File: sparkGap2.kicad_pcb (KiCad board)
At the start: 4 copper layers, 53.1 x 54.1 mm, 47 parts, among them J1 9V, J2 IN, J3 OUT, Q1 BS170, SW1 SPST, SW2 6-pin Footswitch, U1 TL072

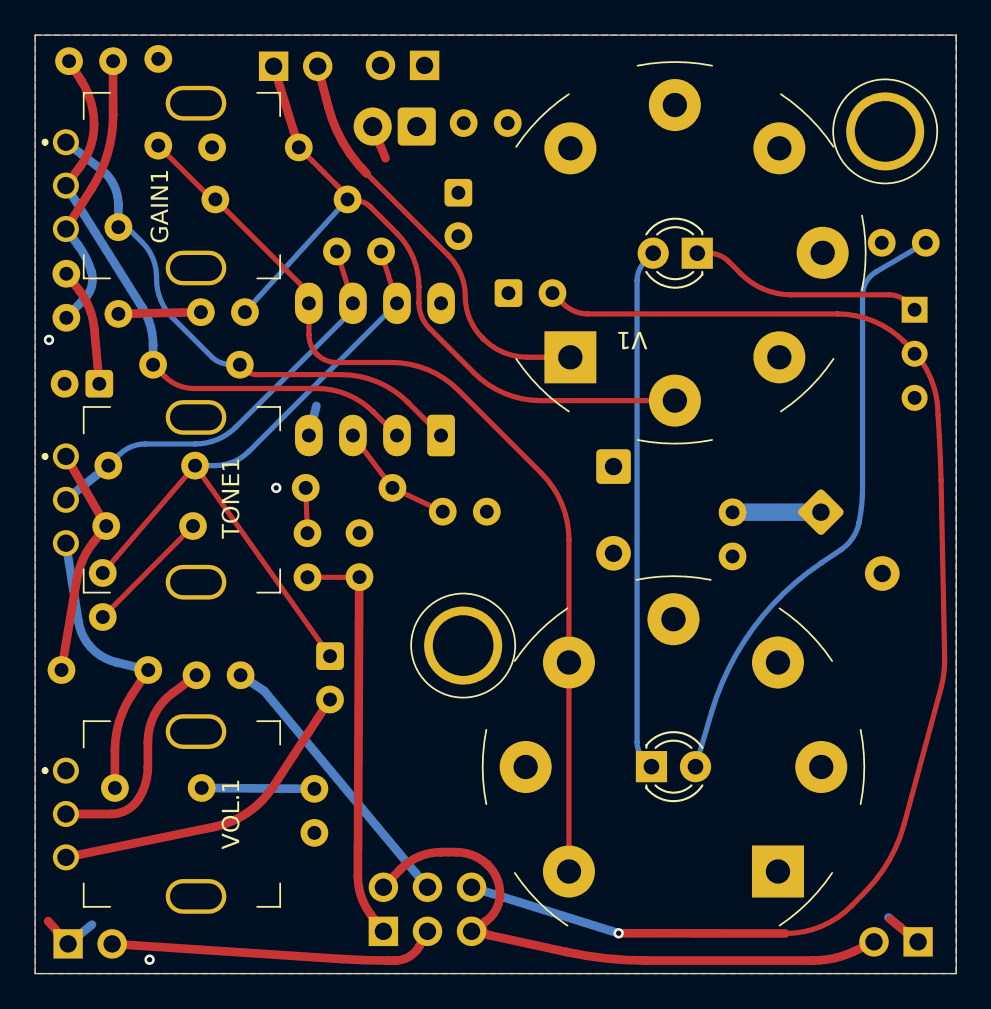
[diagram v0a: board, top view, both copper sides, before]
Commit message: Clean up footprints and schematic to get rid of warnings
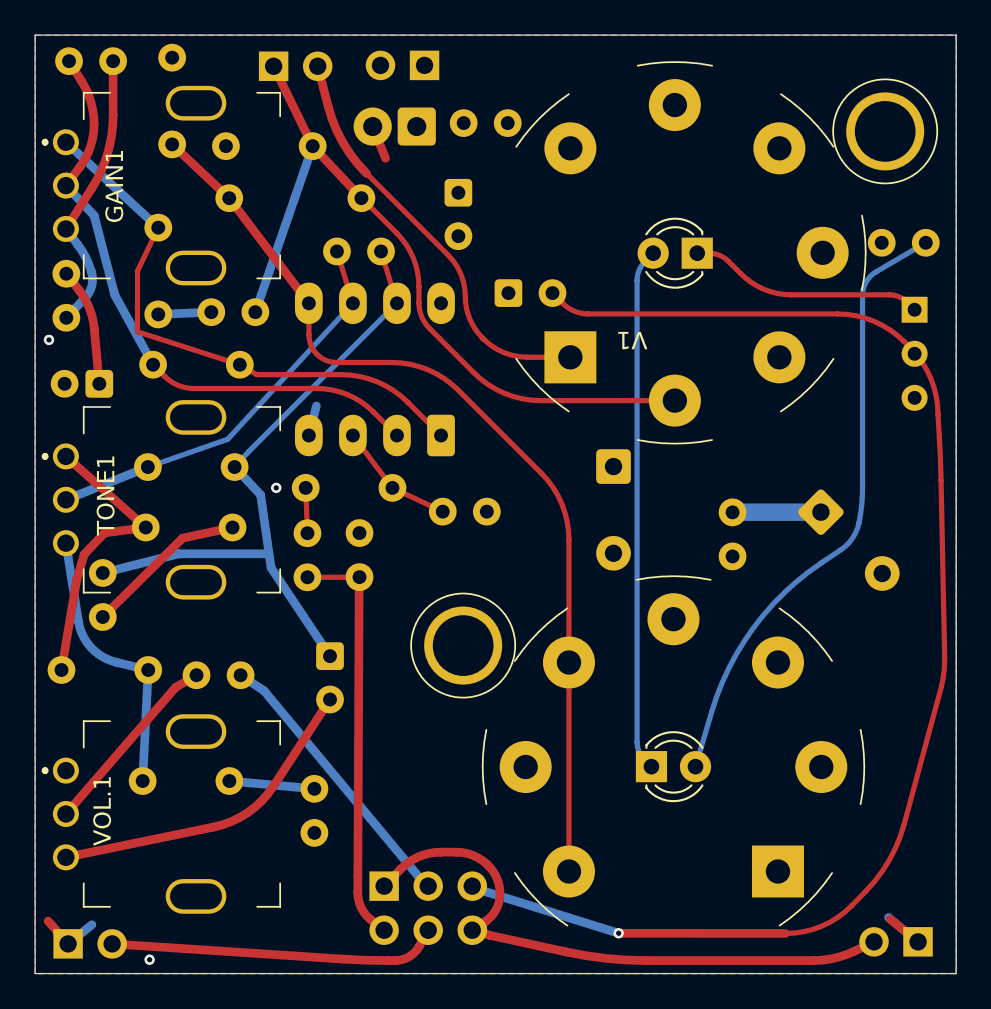
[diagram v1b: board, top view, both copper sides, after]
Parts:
- Mount1, Mount2: renamed from REF**; value B9A-shield-single-mount -> B9A Mount
- SW2: footprint Connector_PinSocket_2.54mm:PinSocket_2x03_P2.54mm_Vertical -> Connector_PinHeader_2.54mm:PinHeader_2x03_P2.54mm_Vertical
- moved SW2 2.60 mm to (40.1, 89.1)
- moved C4 2.30 mm to (27.1, 51.1)
- moved C7 2.28 mm to (31.5, 64.9)
- moved C8 2.28 mm to (31.4, 68.4)
- moved C10 1.65 mm to (26.2, 83.0)
- moved R7 0.80 mm to (38.8, 49.4)
- moved C5 0.80 mm to (36.0, 46.4)
- moved C6 0.80 mm to (27.9, 46.3)
- moved R6 0.60 mm to (30.2, 56.0)
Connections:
- J2 pad 2: Net-(J2-Pad1N) -> Net-(J2-Pad2)
- SW2 pad 1: Net-(R1-Pad1) -> Net-(J3-Pad2)
- SW2 pad 2: Net-(J3-Pad2) -> Net-(R1-Pad1)
- SW2 pad 3: Net-(J2-Pad1N) -> Net-(R11-Pad1)
- SW2 pad 4: Net-(R11-Pad1) -> Net-(J2-Pad2)
- SW2 pad 5: Net-(J3-Pad2) -> Net-(D4-A)
- SW2 pad 6: Net-(D4-A) -> Net-(J3-Pad2)
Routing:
- net Net-(J2-Pad2): track 0.00 -> 19.0 mm
- net Net-(J2-Pad1N): track 19.0 -> 0.00 mm
- net Net-(C8-Pad2): track 14.1 -> 17.1 mm
- net Net-(C2-Pad1): track 30.4 -> 32.7 mm
- net Net-(C8-Pad1): track 7.39 -> 9.41 mm
- net Net-(R11-Pad2): track 12.8 -> 11.1 mm
- net Net-(C4-Pad2): track 4.76 -> 3.06 mm
- net Net-(C10-Pad2): track 6.50 -> 4.92 mm
- net Net-(C11-Pad1): track 40.1 -> 38.6 mm
- net Net-(C10-Pad1): track 17.1 -> 16.2 mm
- net Net-(SW1-A): track 43.6 -> 43.1 mm

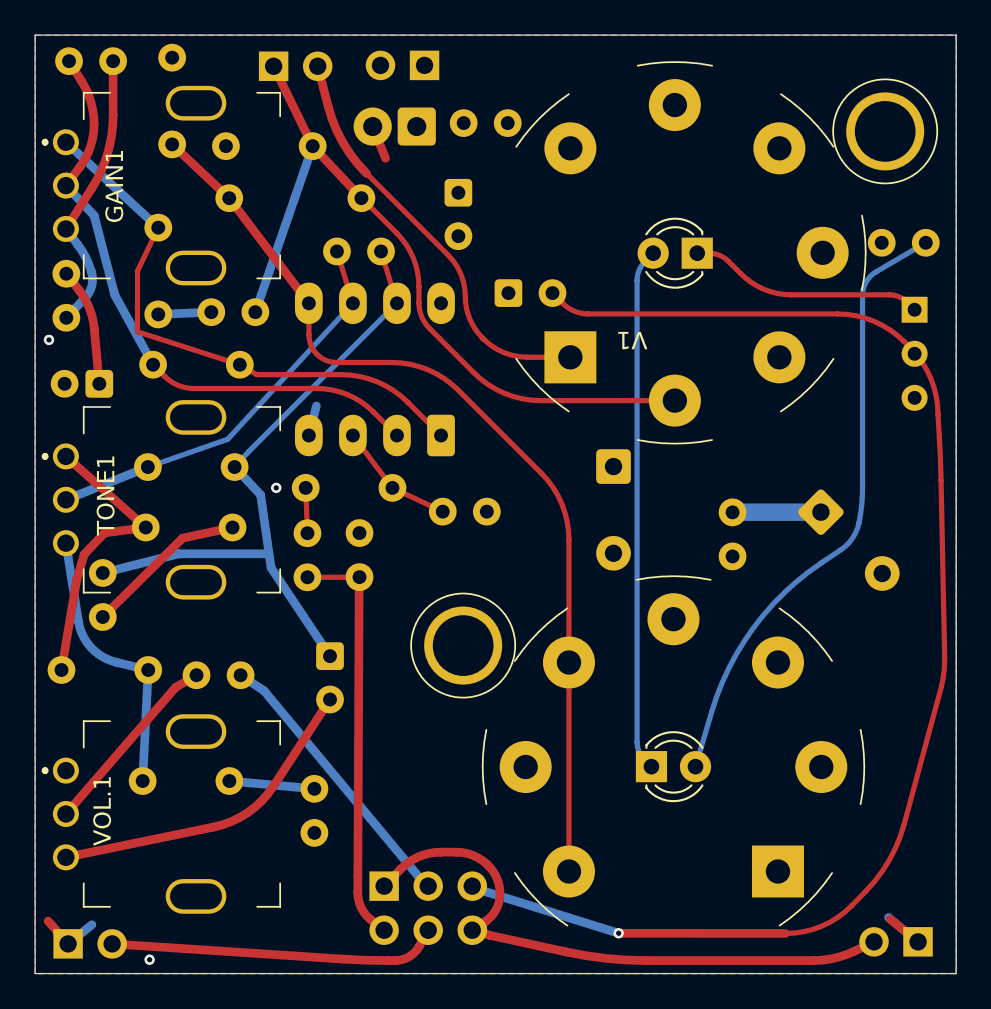
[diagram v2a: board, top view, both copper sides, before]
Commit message: Improve layout to aid in construction, better signal routing, and more visually appealing shield/PCB mounts
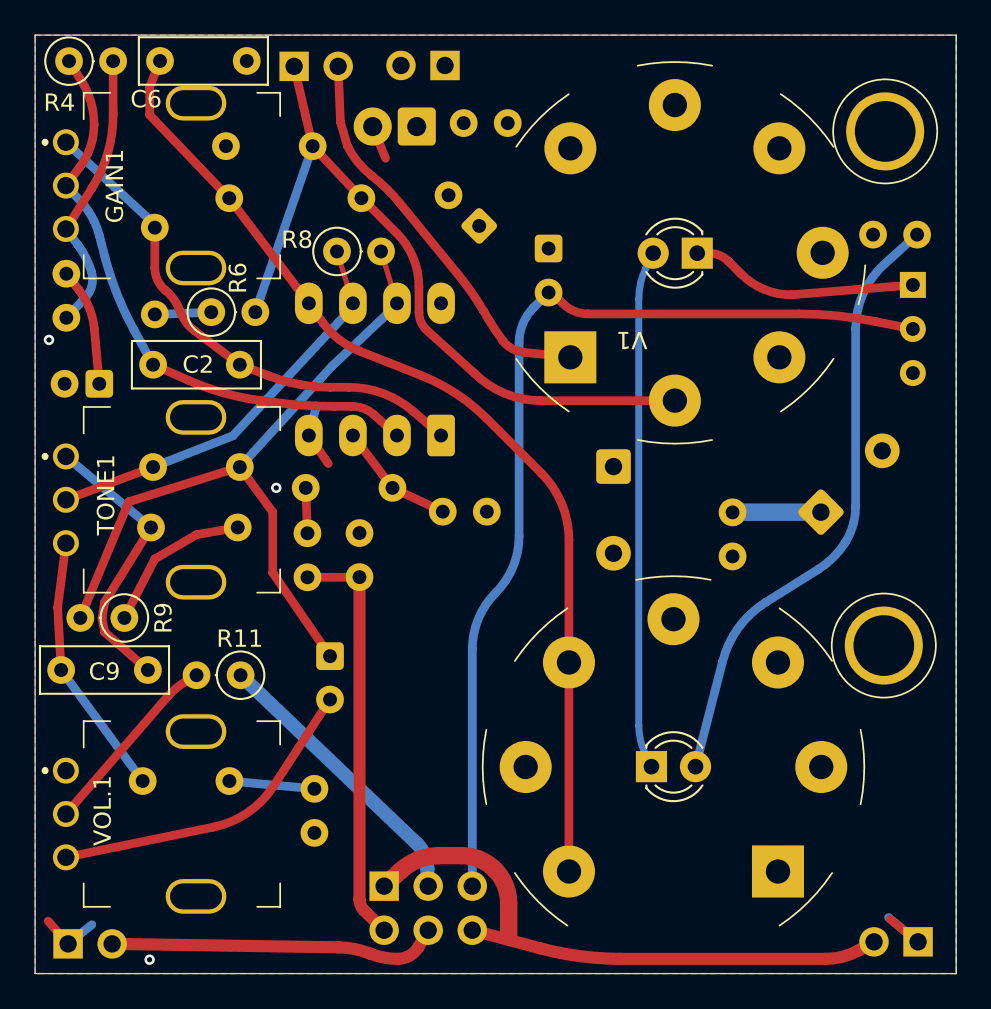
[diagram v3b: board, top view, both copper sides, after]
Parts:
- C2, C6, C9, R11, R4, R6, R8, R9: moved to F.Cu
- moved C9 4.98 mm to (26.5, 76.6), turned to 180 degrees
- moved C6 4.86 mm to (27.2, 41.5), turned to 0 degrees
- moved D4 3.46 mm to (49.6, 52.3), turned to -90 degrees
- moved C13 2.26 mm to (45.6, 51.0), turned to 135 degrees
- moved Q1 1.43 mm to (70.6, 54.4)
- moved R9 1.25 mm to (25.1, 73.6), turned to 180 degrees
- moved J1 1.18 mm to (43.6, 41.8)
- moved SW1 1.18 mm to (34.9, 41.8)
- moved R14 0.69 mm to (70.8, 51.5)
- moved C7 0.30 mm to (31.8, 64.9)
- moved C8 0.30 mm to (31.7, 68.4)
- moved C4 0.20 mm to (26.9, 51.1)
- turned C14 to 45 degrees
- turned Mount2 to -60 degrees
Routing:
- net Net-(D4-A): track 78.1 -> 56.7 mm, vias 1 -> 0
- net Net-(C11-Pad1): track 38.6 -> 42.7 mm
- net A: track 74.6 -> 70.6 mm
- net Net-(U1B-+): track 54.8 -> 58.6 mm
- net Net-(C2-Pad1): track 32.7 -> 29.8 mm
- net Earth: track 15.1 -> 17.1 mm
- net Net-(SW1-B): track 24.2 -> 23.2 mm
- net Net-(C10-Pad1): track 16.2 -> 15.3 mm
- net Net-(J3-Pad2): track 34.1 -> 34.8 mm
- net Net-(C8-Pad2): track 17.1 -> 16.5 mm
